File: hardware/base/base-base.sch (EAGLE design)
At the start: 30 parts, among them U1 SD_CARD_SOCKET4UCON, X1 BU-SMA-V

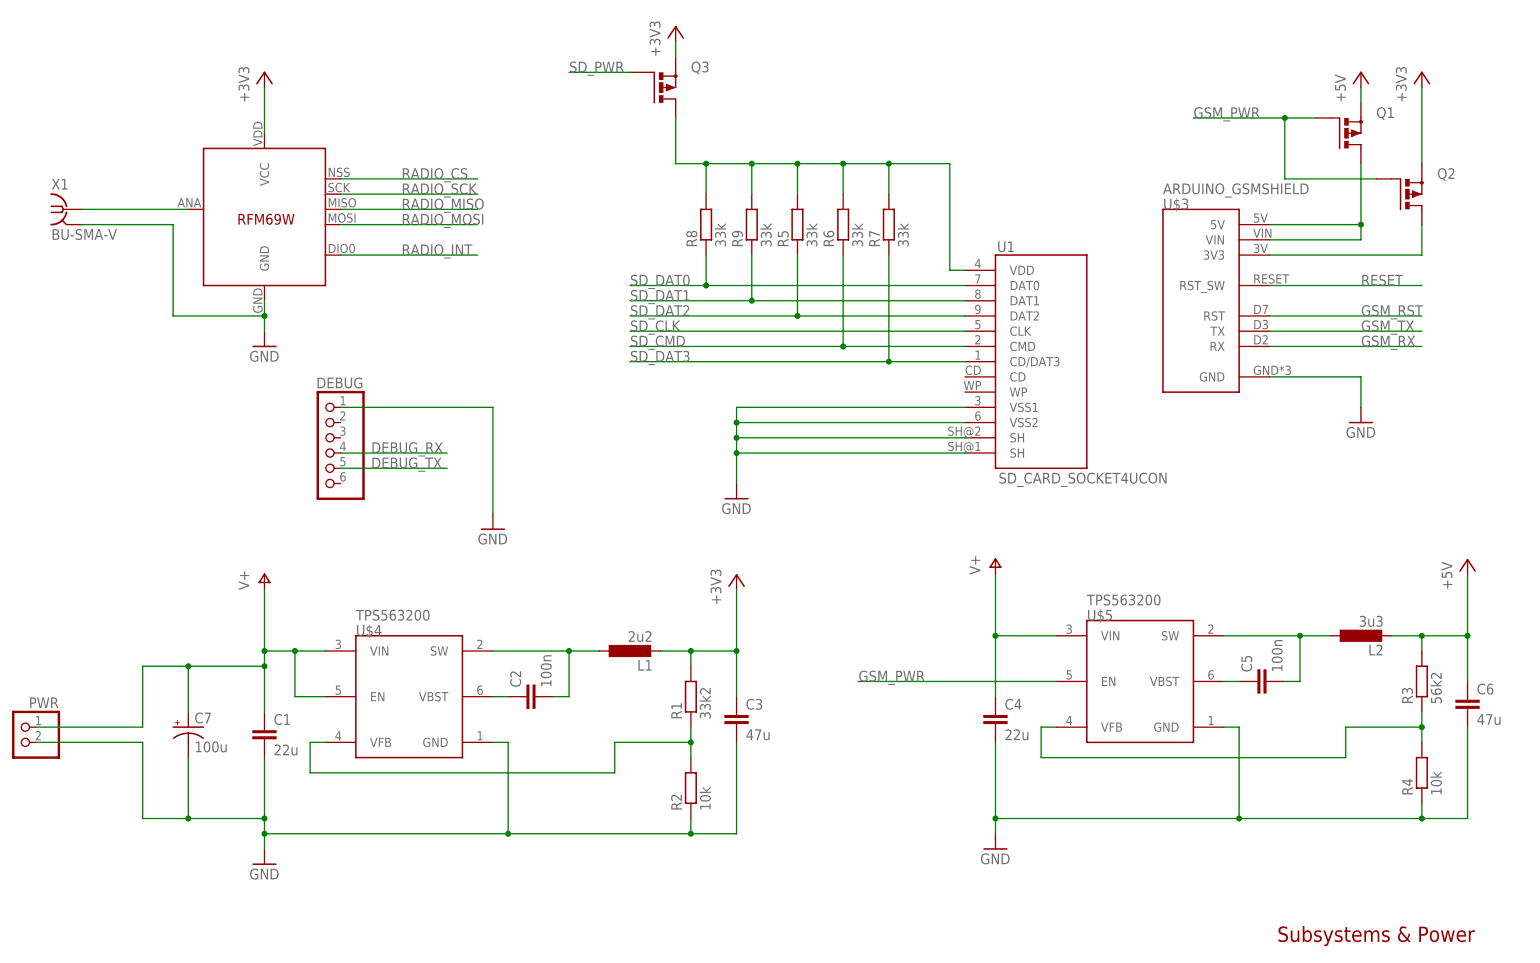
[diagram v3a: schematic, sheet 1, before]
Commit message: BASEHW: New inductors, larger resistors
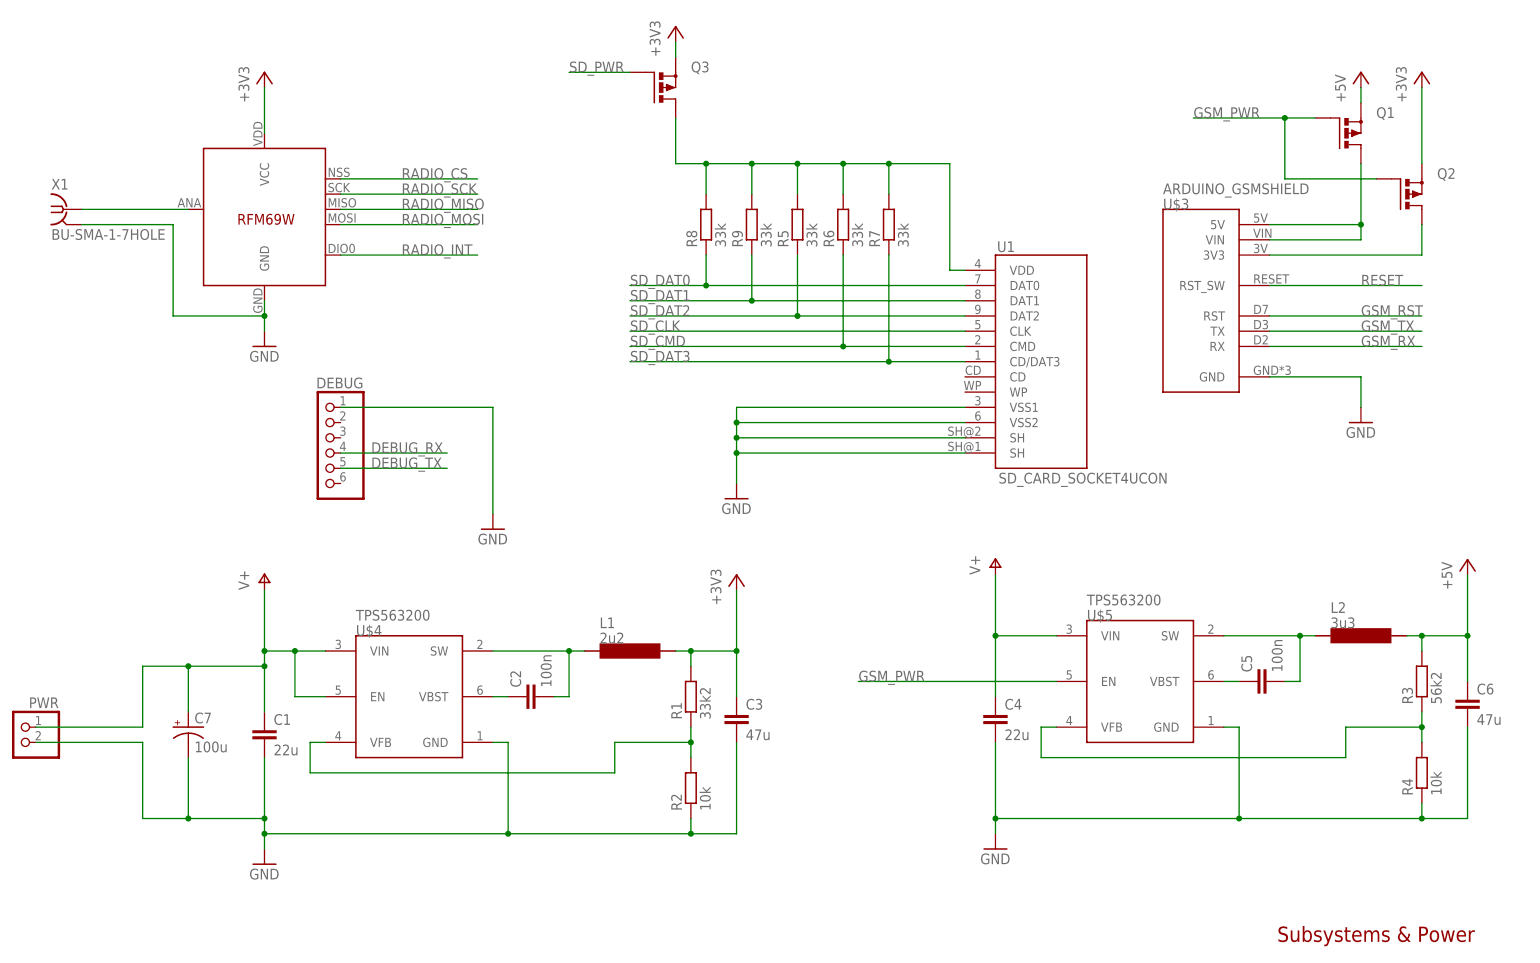
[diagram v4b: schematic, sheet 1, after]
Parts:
- L1, L2: device resistor:L-EU0207/2V -> FullyCustom:SRR7032
- R1, R2, R3, R4, R5, R6, R7, R8, R9: device resistor:R-EU_0204/5 -> resistor:R-EU_0204/7
- X1: value BU-SMA-V -> BU-SMA-1-7HOLE; device con-coax:BU-SMA-V -> FullyCustom:BU-SMA-1-7HOLE
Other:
- moved on the sheet: L1, L2

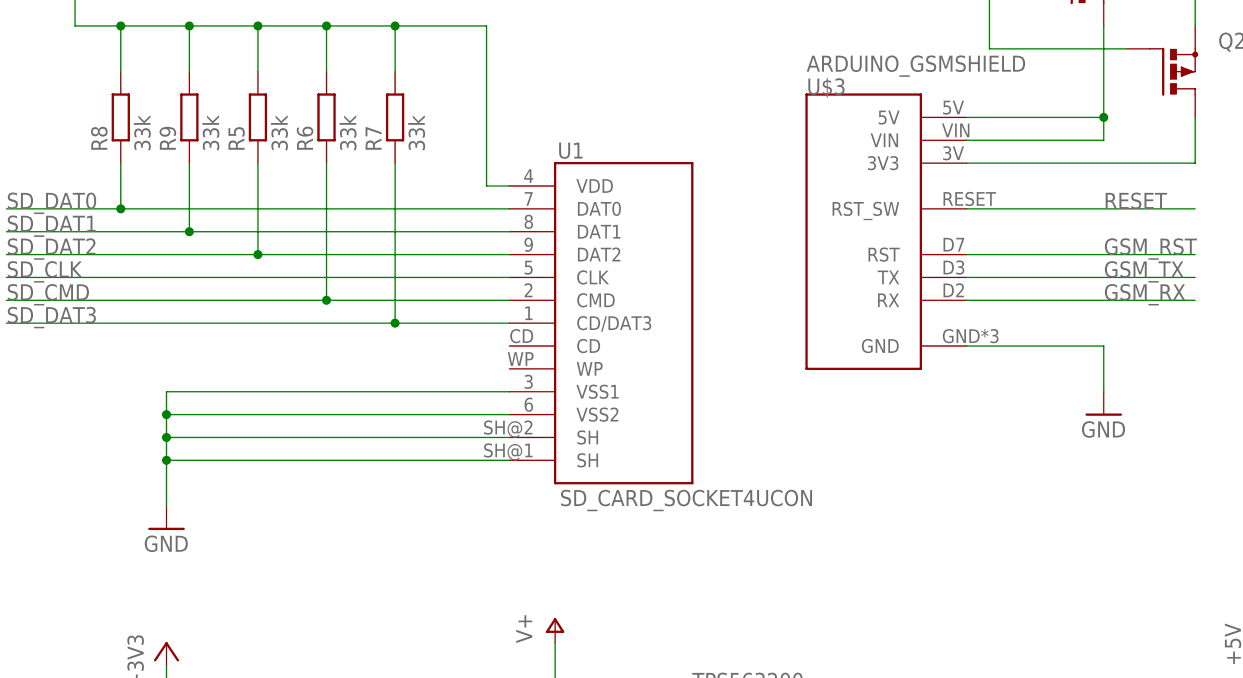
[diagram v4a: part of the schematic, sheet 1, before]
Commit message: BASEHW: New SD footprint
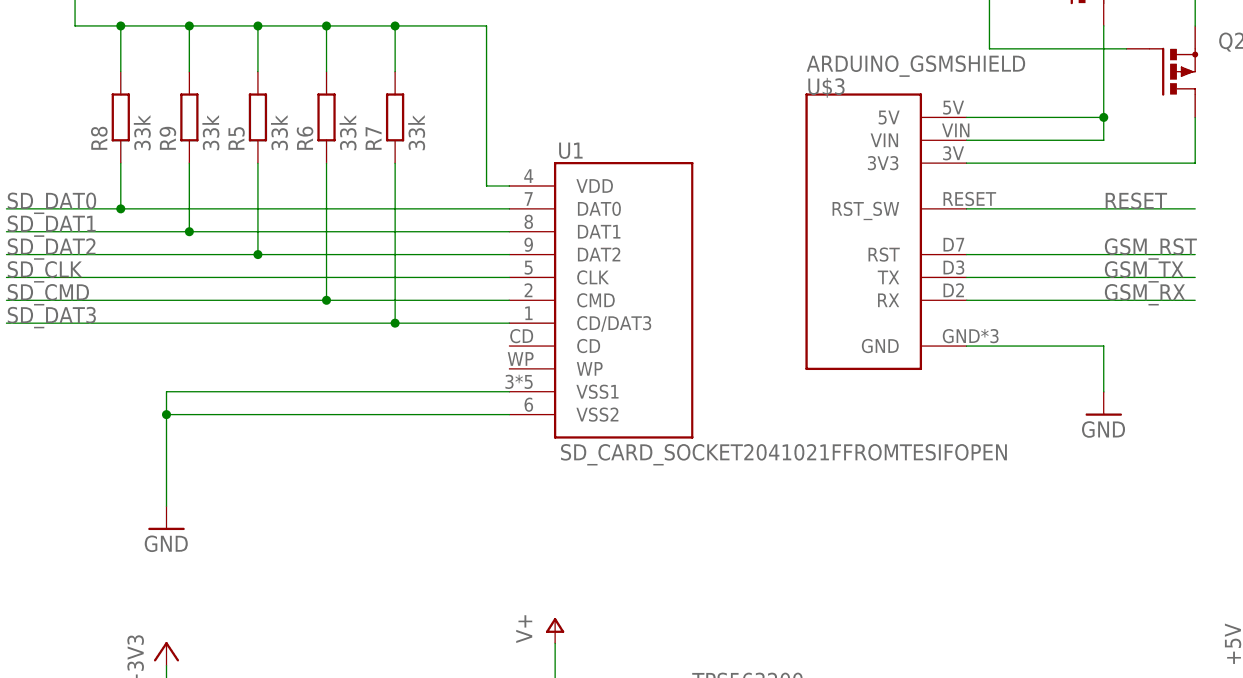
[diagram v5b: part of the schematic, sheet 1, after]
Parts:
- U1: value SD_CARD_SOCKET4UCON -> SD_CARD_SOCKET2041021FFROMTESIFOPEN; device SparkFun-Connectors:SD_CARD_SOCKET4UCON -> FullyCustom:SD_CARD_SOCKET2041021FFROMTESIFOPEN
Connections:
- net GND: no longer U1.SH@1, U1.SH@2
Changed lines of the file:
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@@
 <part name="GND5" library="supply1" deviceset="GND" device=""/>
 <part name="X1" library="FullyCustom" deviceset="BU-SMA-1-7HOLE" device=""/>
-<part name="U1" library="SparkFun-Connectors" deviceset="SD_CARD_SOCKET" device="4UCON"/>
+<part name="U1" library="FullyCustom" deviceset="SD_CARD_SOCKET" device="2041021FFROMTESIFOPEN"/>
 <part name="GND6" library="supply1" deviceset="GND" device=""/>
 <part name="+3V6" library="supply1" deviceset="+3V3" device=""/>
@@
 <wire x1="127" y1="109.22" x2="127" y2="106.68" width="0.1524" layer="91"/>
 <pinref part="U1" gate="G$1" pin="VSS2"/>
-<wire x1="127" y1="106.68" x2="127" y2="104.14" width="0.1524" layer="91"/>
-<wire x1="127" y1="104.14" x2="127" y2="101.6" width="0.1524" layer="91"/>
-<wire x1="127" y1="101.6" x2="127" y2="96.52" width="0.1524" layer="91"/>
+<wire x1="127" y1="106.68" x2="127" y2="96.52" width="0.1524" layer="91"/>
 <wire x1="165.1" y1="106.68" x2="127" y2="106.68" width="0.1524" layer="91"/>
 <junction x="127" y="106.68"/>
-<pinref part="U1" gate="G$1" pin="SH@2"/>
-<wire x1="165.1" y1="104.14" x2="127" y2="104.14" width="0.1524" layer="91"/>
-<junction x="127" y="104.14"/>
-<pinref part="U1" gate="G$1" pin="SH@1"/>
-<wire x1="165.1" y1="101.6" x2="127" y2="101.6" width="0.1524" layer="91"/>
-<junction x="127" y="101.6"/>
 </segment>
 <segment>
